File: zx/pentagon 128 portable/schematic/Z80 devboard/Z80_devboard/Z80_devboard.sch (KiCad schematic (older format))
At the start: 5 parts

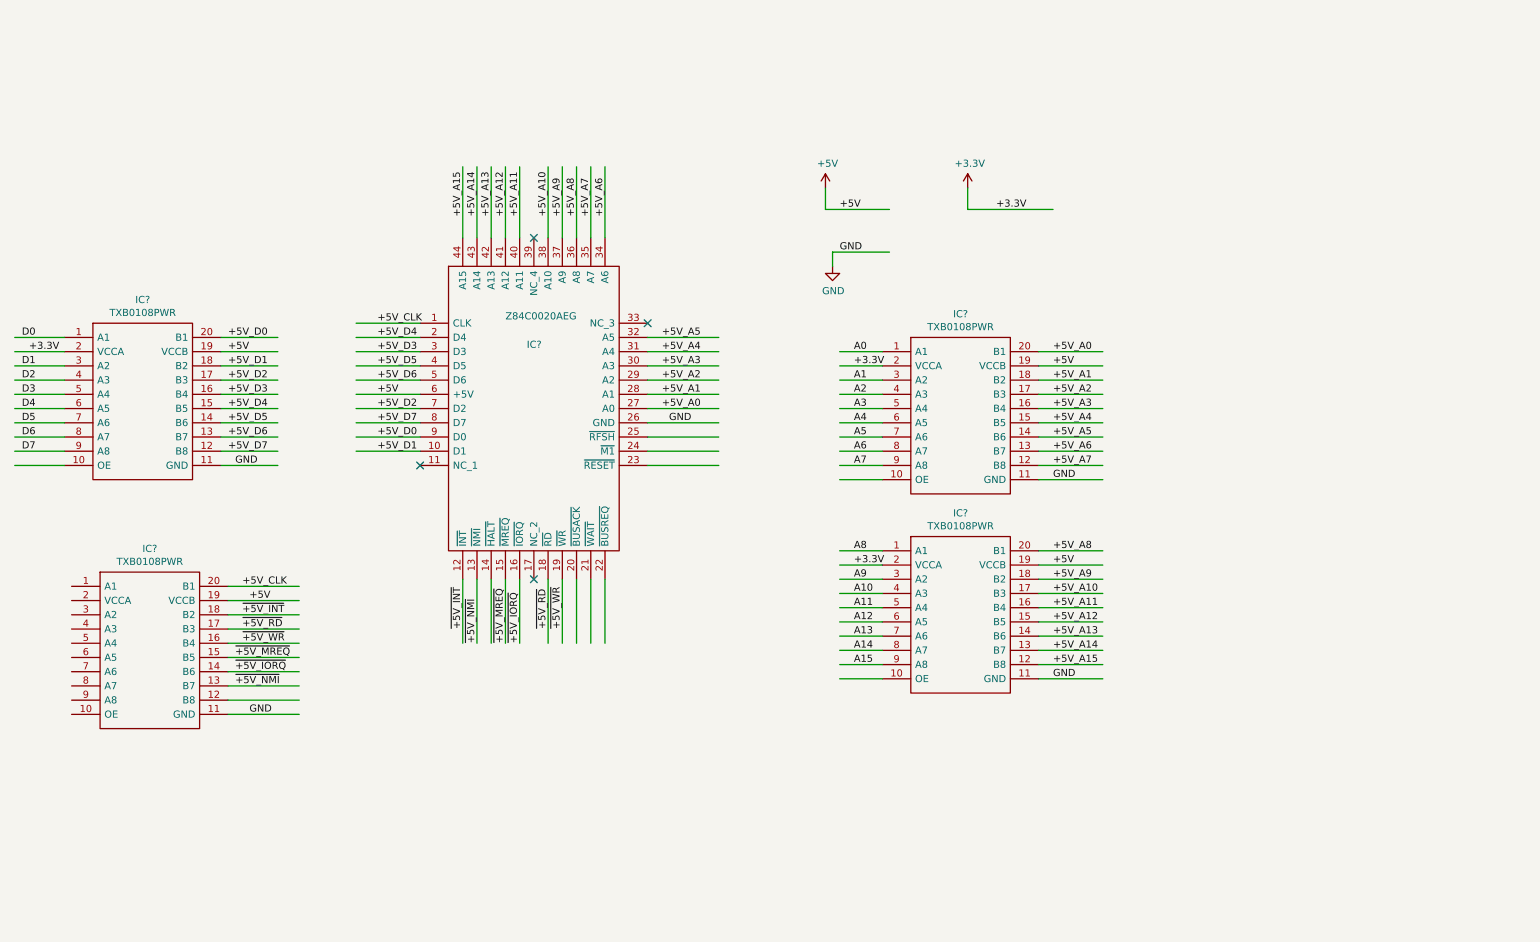
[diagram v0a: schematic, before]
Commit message: added ZX Keyboard
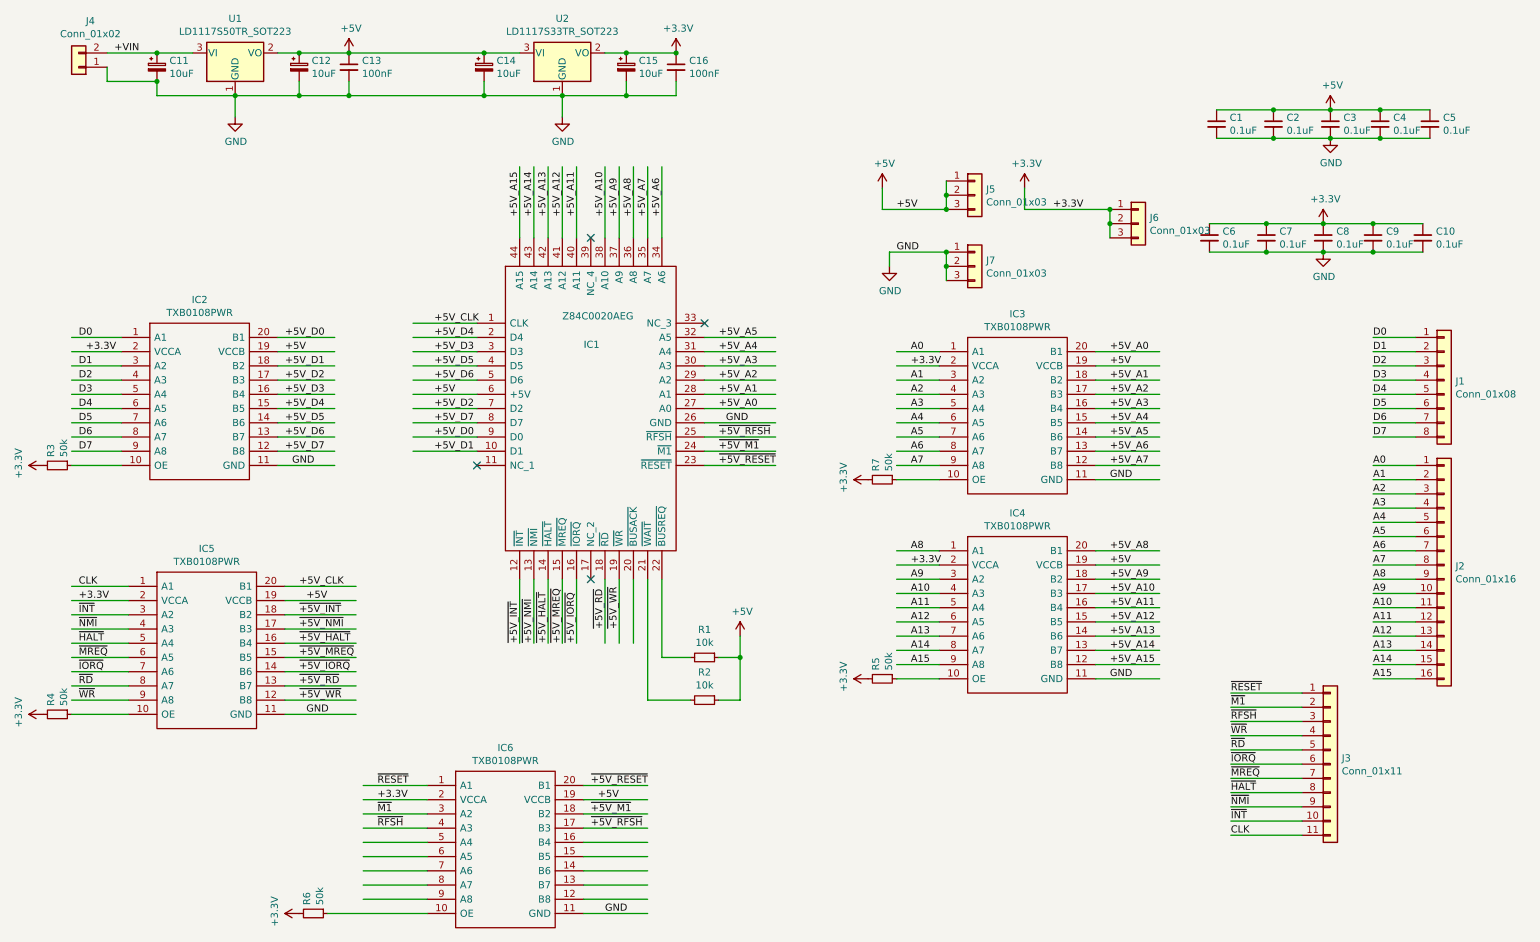
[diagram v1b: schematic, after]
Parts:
- added C1, C10, C2, C3, C4, C5, C6, C7, C8, C9: 0.1uF, Capacitor_SMD:C_0402_1005Metric, symbol Device:C_Small
- added C11, C12, C14, C15: 10uF, Capacitor_SMD:C_0402_1005Metric, symbol Device:CP_Small
- added C13, C16: 100nF, Capacitor_SMD:C_0402_1005Metric, symbol Device:C_Small
- added IC6: TXB0108PWR, SamacSys_Parts:SOP65P640X120-20N, symbol SamacSys_Parts:TXB0108PWR
- added J1: Conn_01x08, Connector_PinHeader_2.54mm:PinHeader_1x08_P2.54mm_Vertical, symbol Connector_Generic:Conn_01x08
- added J2: Conn_01x16, Connector_PinHeader_2.54mm:PinHeader_1x16_P2.54mm_Vertical, symbol Connector_Generic:Conn_01x16
- added J3: Conn_01x11, Connector_PinHeader_2.54mm:PinHeader_1x11_P2.54mm_Vertical, symbol Connector_Generic:Conn_01x11
- added J4: Conn_01x02, Connector_PinHeader_2.54mm:PinHeader_1x02_P2.54mm_Vertical, symbol Connector_Generic:Conn_01x02
- added J5, J6, J7: Conn_01x03, Connector_PinHeader_2.54mm:PinHeader_1x03_P2.54mm_Vertical, symbol Connector_Generic:Conn_01x03
- added R1, R2: 10k, Resistor_SMD:R_0402_1005Metric, symbol Device:R_Small
- added R3, R4, R5, R6, R7: 50k, Resistor_SMD:R_0402_1005Metric, symbol Device:R_Small
- added U1: LD1117S50TR_SOT223, Package_TO_SOT_SMD:SOT-223-3_TabPin2, symbol Regulator_Linear:LD1117S50TR_SOT223
- added U2: LD1117S33TR_SOT223, Package_TO_SOT_SMD:SOT-223-3_TabPin2, symbol Regulator_Linear:LD1117S33TR_SOT223
- IC1: renamed from IC?; footprint QFP80P1200X1200X160-44N -> SamacSys_Parts:QFP80P1200X1200X160-44N
- IC2, IC3, IC4, IC5: renamed from IC?; footprint SOP65P640X120-20N -> SamacSys_Parts:SOP65P640X120-20N
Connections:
- net labels added: +VIN, CLK, ~+5V_HALT, ~+5V_M1, ~+5V_RESET, ~+5V_RFSH, ~HALT, ~INT, ~IORQ, ~M1, ~MREQ, ~NMI, ~RD, ~RESET, ~RFSH, ~WR
- wire segments 116 -> 234
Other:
- moved on the sheet: IC1, IC2, IC3, IC4, IC5
